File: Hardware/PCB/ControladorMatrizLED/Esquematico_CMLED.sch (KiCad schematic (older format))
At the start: 4 parts

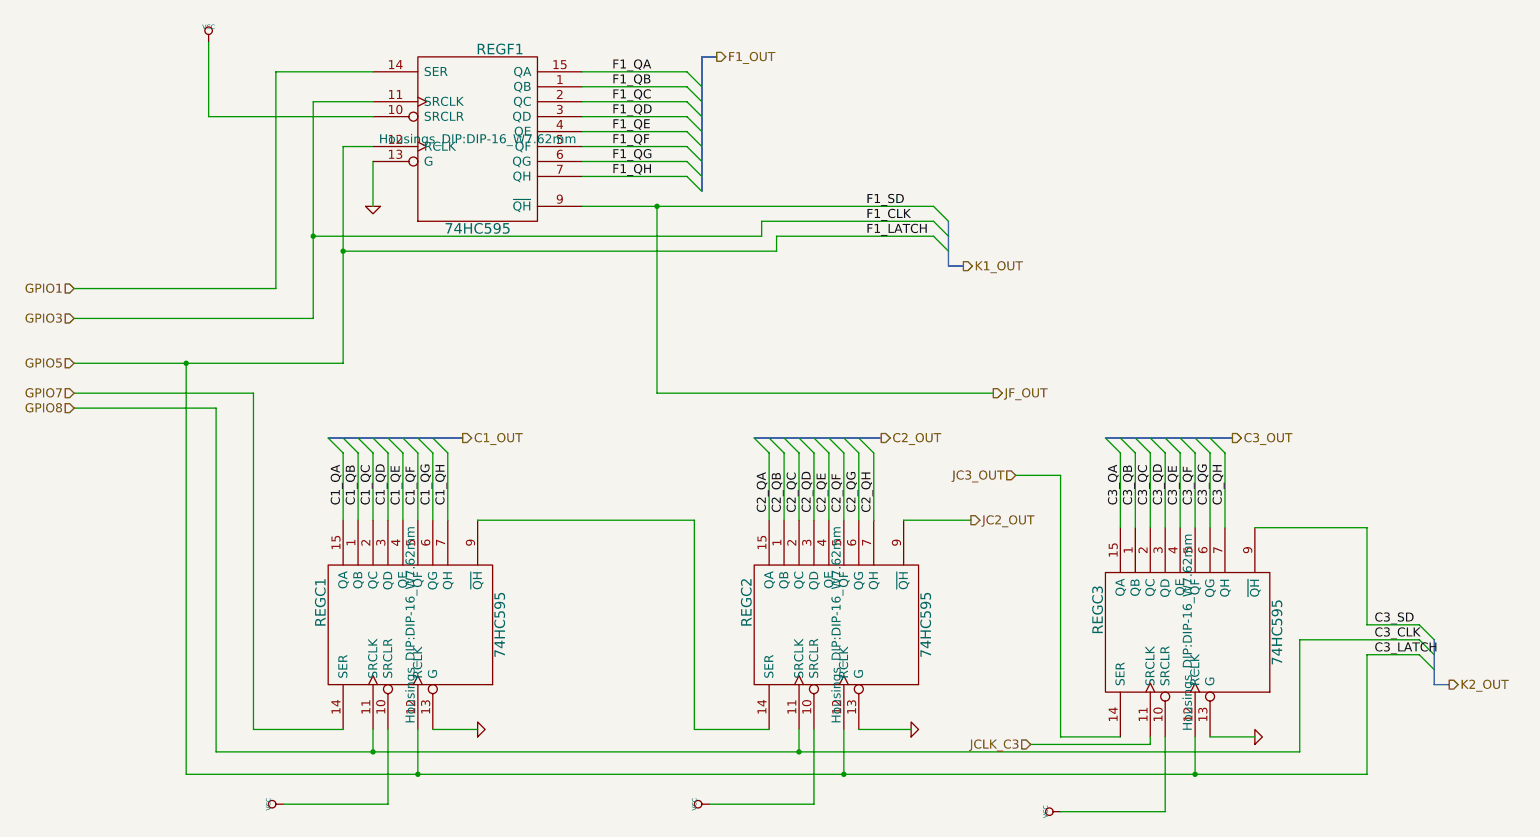
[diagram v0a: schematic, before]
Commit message: Avance sobre Esquematico y PCB - Pistas terminadas
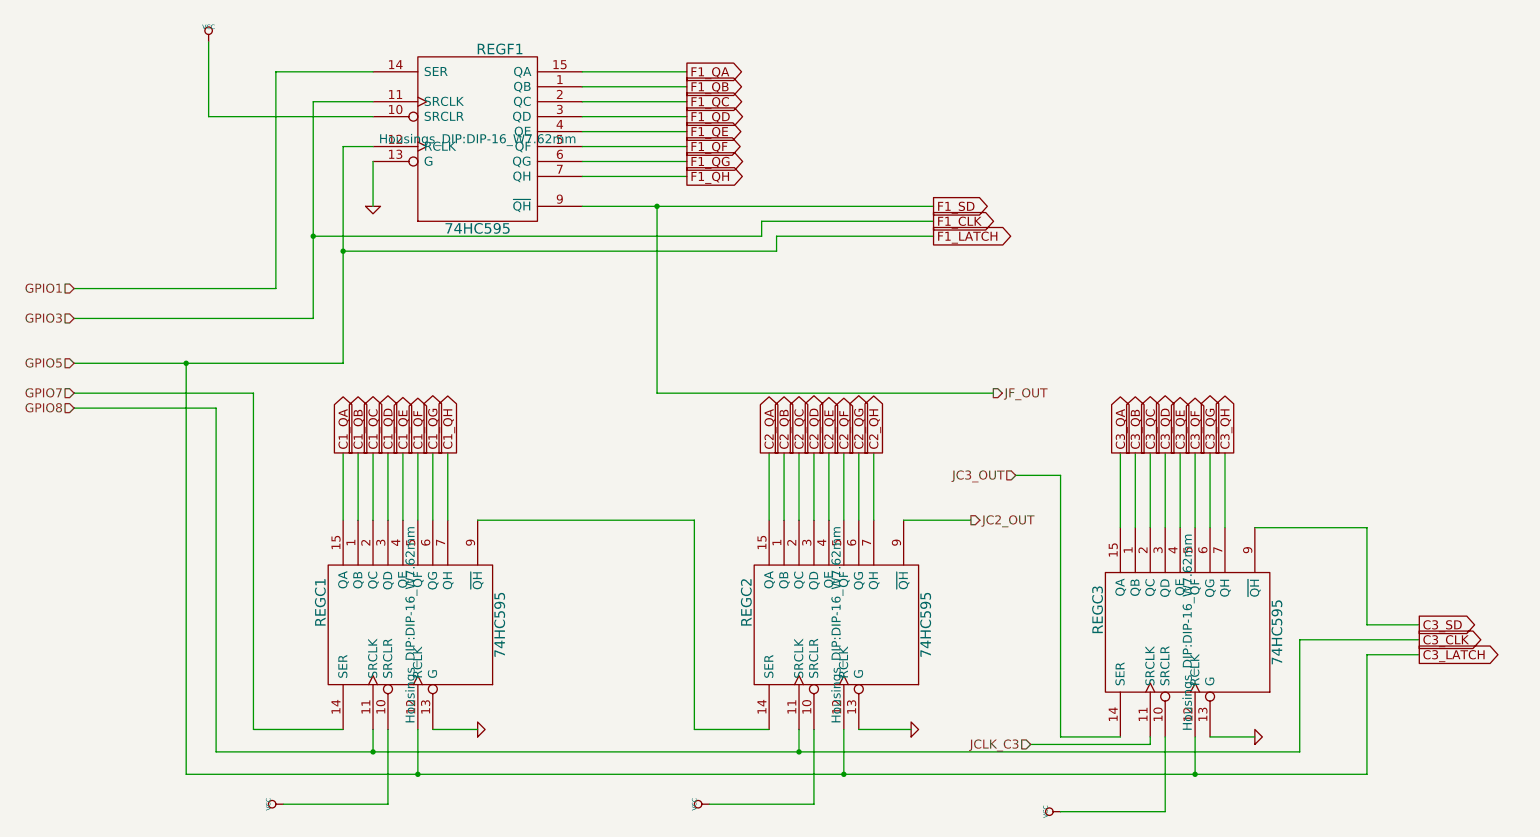
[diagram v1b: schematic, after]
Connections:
- net GPIO3 renamed F1_CLK
- net GPIO5 renamed C3_LATCH
- net GPIO8 renamed C3_CLK
- net JF_OUT renamed F1_SD

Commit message: Actualizacion con modelo poncho grande y LCD
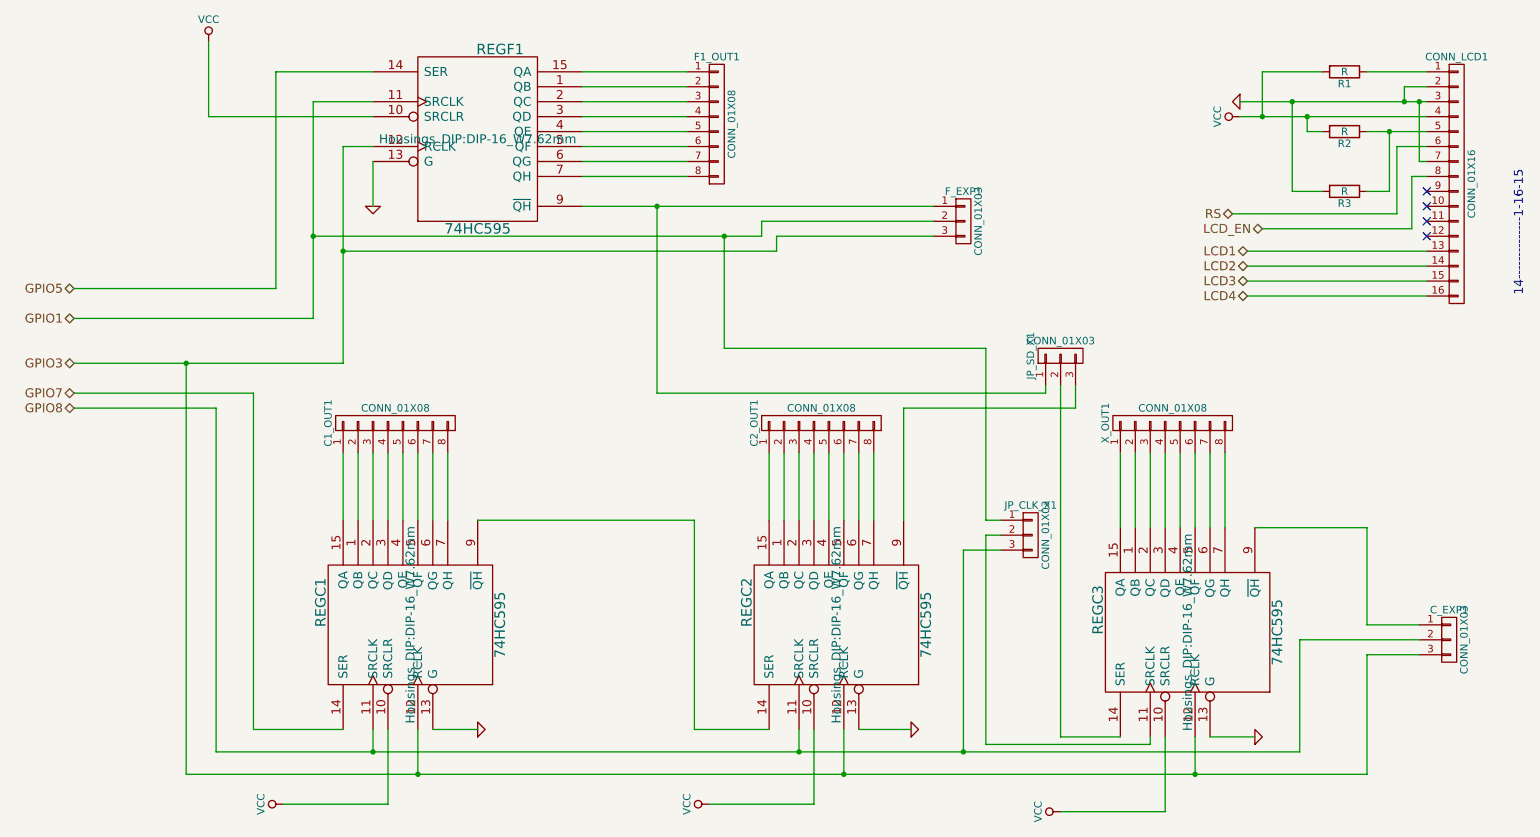
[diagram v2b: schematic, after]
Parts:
- added C1_OUT1, C2_OUT1, F1_OUT1, X_OUT1: CONN_01X08, Socket_Strips:Socket_Strip_Straight_1x08, symbol CONN_01X08
- added CONN_LCD1: CONN_01X16, Socket_Strips:Socket_Strip_Straight_1x16, symbol CONN_01X16
- added C_EXP1, F_EXP1, JP_CLK_X1, JP_SD_X1: CONN_01X03, Socket_Strips:Socket_Strip_Straight_1x03, symbol CONN_01X03
- added R1, R2, R3: R, Resistors_ThroughHole:Resistor_Horizontal_RM10mm, symbol R
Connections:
- net F1_CLK is gone; now on net GPIO1: REGF1.11 (SRCLK)
- net GND: now also CONN_LCD1.2 (P2), CONN_LCD1.3 (P3), CONN_LCD1.7 (P7), R3.2
- net GPIO1: now also F_EXP1.2 (P2), JP_CLK_X1.1 (P1); no longer REGF1.14 (SER)
- net VCC: now also CONN_LCD1.4 (P4), R1.2, R2.2
- net C1_QA: no longer names the net of REGC1.15 (QA)
- net C1_QA: now also C1_OUT1.1 (P1)
- net C1_QB: no longer names the net of REGC1.1 (QB)
- net C1_QB: now also C1_OUT1.2 (P2)
- net C1_QC: no longer names the net of REGC1.2 (QC)
- net C1_QC: now also C1_OUT1.3 (P3)
- net C1_QD: no longer names the net of REGC1.3 (QD)
- net C1_QD: now also C1_OUT1.4 (P4)
- net C1_QE: no longer names the net of REGC1.4 (QE)
- net C1_QE: now also C1_OUT1.5 (P5)
- net C1_QF: no longer names the net of REGC1.5 (QF)
- net C1_QF: now also C1_OUT1.6 (P6)
- net C1_QG: no longer names the net of REGC1.6 (QG)
- net C1_QG: now also C1_OUT1.7 (P7)
- net C1_QH: no longer names the net of REGC1.7 (QH)
- net C1_QH: now also C1_OUT1.8 (P8)
- net C2_QA: no longer names the net of REGC2.15 (QA)
- net C2_QA: now also C2_OUT1.1 (P1)
- net C2_QB: no longer names the net of REGC2.1 (QB)
- net C2_QB: now also C2_OUT1.2 (P2)
- net C2_QC: no longer names the net of REGC2.2 (QC)
- net C2_QC: now also C2_OUT1.3 (P3)
- net C2_QD: no longer names the net of REGC2.3 (QD)
- net C2_QD: now also C2_OUT1.4 (P4)
- net C2_QE: no longer names the net of REGC2.4 (QE)
- net C2_QE: now also C2_OUT1.5 (P5)
- net C2_QF: no longer names the net of REGC2.5 (QF)
- net C2_QF: now also C2_OUT1.6 (P6)
- net C2_QG: no longer names the net of REGC2.6 (QG)
- net C2_QG: now also C2_OUT1.7 (P7)
- net C2_QH: no longer names the net of REGC2.7 (QH)
- net C2_QH: now also C2_OUT1.8 (P8)
- net C3_CLK renamed GPIO8
- net GPIO8: now also C_EXP1.2 (P2), JP_CLK_X1.3 (P3)
- net C3_LATCH renamed GPIO3
- net GPIO3: now also C_EXP1.3 (P3), F_EXP1.3 (P3)
- net C3_QA: no longer names the net of REGC3.15 (QA)
- net C3_QA: now also X_OUT1.1 (P1)
- net C3_QB: no longer names the net of REGC3.1 (QB)
- net C3_QB: now also X_OUT1.2 (P2)
- net C3_QC: no longer names the net of REGC3.2 (QC)
- net C3_QC: now also X_OUT1.3 (P3)
- net C3_QD: no longer names the net of REGC3.3 (QD)
- net C3_QD: now also X_OUT1.4 (P4)
- net C3_QE: no longer names the net of REGC3.4 (QE)
- net C3_QE: now also X_OUT1.5 (P5)
- net C3_QF: no longer names the net of REGC3.5 (QF)
- net C3_QF: now also X_OUT1.6 (P6)
- net C3_QG: no longer names the net of REGC3.6 (QG)
- net C3_QG: now also X_OUT1.7 (P7)
- net C3_QH: no longer names the net of REGC3.7 (QH)
- net C3_QH: now also X_OUT1.8 (P8)
- net C3_SD: no longer names the net of REGC3.9 (~QH)
- net C3_SD: now also C_EXP1.1 (P1)
- net F1_QA: no longer names the net of REGF1.15 (QA)
- net F1_QA: now also F1_OUT1.1 (P1)
- net F1_QB: no longer names the net of REGF1.1 (QB)
- net F1_QB: now also F1_OUT1.2 (P2)
- net F1_QC: no longer names the net of REGF1.2 (QC)
- net F1_QC: now also F1_OUT1.3 (P3)
- net F1_QD: no longer names the net of REGF1.3 (QD)
- net F1_QD: now also F1_OUT1.4 (P4)
- net F1_QE: no longer names the net of REGF1.4 (QE)
- net F1_QE: now also F1_OUT1.5 (P5)
- net F1_QF: no longer names the net of REGF1.5 (QF)
- net F1_QF: now also F1_OUT1.6 (P6)
- net F1_QG: no longer names the net of REGF1.6 (QG)
- net F1_QG: now also F1_OUT1.7 (P7)
- net F1_QH: no longer names the net of REGF1.7 (QH)
- net F1_QH: now also F1_OUT1.8 (P8)
- net F1_SD: no longer names the net of REGF1.9 (~QH)
- net F1_SD: now also F_EXP1.1 (P1), JP_SD_X1.1 (P1)
- net JC2_OUT: no longer names the net of REGC2.9 (~QH)
- net JC2_OUT: now also JP_SD_X1.3 (P3)
- net JC3_OUT: no longer names the net of REGC3.14 (SER)
- net JC3_OUT: now also JP_SD_X1.2 (P2)
- net JCLK_C3: no longer names the net of REGC3.11 (SRCLK)
- net JCLK_C3: now also JP_CLK_X1.2 (P2)
- new net: CONN_LCD1.1 (P1), R1.1
- new net: CONN_LCD1.5 (P5), R2.1, R3.1
- new net GPIO5: REGF1.14 (SER)
- new net LCD1: CONN_LCD1.13 (P13)
- new net LCD2: CONN_LCD1.14 (P14)
- new net LCD3: CONN_LCD1.15 (P15)
- new net LCD4: CONN_LCD1.16 (P16)
- new net LCD_EN: CONN_LCD1.8 (P8)
- new net RS: CONN_LCD1.6 (P6)
- no-connect marks 0 -> 4
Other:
- note added: "14--------------1-16-15"
